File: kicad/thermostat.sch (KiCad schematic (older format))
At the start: 18 parts, among them J1 Display i2c, J2 Sensor i2c, J3 PoE Input, J4 PoE Output, J5 1827585-1

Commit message: Ready for checkout and routing
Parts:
- removed J5: 1827585-1, TE_1827585-1, symbol thermostat:1827585-1
- added J5: 0857891001, project_footprints:0857891001, symbol thermostat:0857891001
- J1: footprint Socket_Strips:Socket_Strip_Angled_1x04_Pitch2.54mm -> Pin_Headers:Pin_Header_Angled_1x04_Pitch2.54mm
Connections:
- net GND: now also J4.1 (Pin_1)
- net PWR_3.3V: no longer SW_DOWN1.2, SW_ENTER1.2, SW_MODE1.2, SW_UP1.2
- net PWR_5V: now also J4.2 (Pin_2), SW_DOWN1.2, SW_ENTER1.2, SW_MODE1.2, SW_UP1.2
- net at J3.1 (Pin_1): now also J5.17 (J11)
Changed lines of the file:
@@
 EESchema Schematic File Version 4
 LIBS:thermostat-cache
-EELAYER 30 0
+EELAYER 29 0
 EELAYER END
 $Descr A4 11693 8268
@@
 	2100 5650 2500 5650
 Text Label 2500 5650 0    50   ~ 0
-PWR_3.3V
+PWR_5V
 Text Label 2500 5200 0    50   ~ 0
-PWR_3.3V
+PWR_5V
 Text Label 2500 4750 0    50   ~ 0
-PWR_3.3V
+PWR_5V
 Text Label 2500 4300 0    50   ~ 0
-PWR_3.3V
+PWR_5V
 Wire Wire Line
 	1700 5650 850  5650
@@
 F 0 "J1" H 9580 3092 50  0000 L CNN
 F 1 "Display i2c" H 9580 3001 50  0000 L CNN
-F 2 "Socket_Strips:Socket_Strip_Angled_1x04_Pitch2.54mm" H 9500 3100 50  0001 C CNN
+F 2 "Pin_Headers:Pin_Header_Angled_1x04_Pitch2.54mm" H 9500 3100 50  0001 C CNN
 F 3 "~" H 9500 3100 50  0001 C CNN
 	1    9500 3100
@@
 F 3 "~" H 9500 3600 50  0001 C CNN
 	1    9500 3600
-	1    0    0    -1
-$EndComp
-$Comp
-L Connector_Generic:Conn_01x04 J3
-U 1 1 5D685426
-P 4850 5700
-F 0 "J3" H 4930 5692 50  0000 L CNN
-F 1 "PoE Input" H 4930 5601 50  0000 L CNN
-F 2 "Socket_Strips:Socket_Strip_Angled_1x04_Pitch2.54mm" H 4850 5700 50  0001 C CNN
-F 3 "~" H 4850 5700 50  0001 C CNN
-	1    4850 5700
-	-1   0    0    1
-$EndComp
-$Comp
-L Connector_Generic:Conn_01x04 J4
-U 1 1 5D687A2E
-P 4850 5100
-F 0 "J4" H 4930 5092 50  0000 L CNN
-F 1 "PoE Output" H 4930 5001 50  0000 L CNN
-F 2 "Socket_Strips:Socket_Strip_Angled_1x04_Pitch2.54mm" H 4850 5100 50  0001 C CNN
-F 3 "~" H 4850 5100 50  0001 C CNN
-	1    4850 5100
-	-1   0    0    1
-$EndComp
-$Comp
-L thermostat:1827585-1 J5
-U 1 1 5D644363
-P 5750 5350
-F 0 "J5" H 6029 5363 50  0000 L CNN
-F 1 "1827585-1" H 6029 5272 50  0000 L CNN
-F 2 "TE_1827585-1" H 5750 5350 50  0001 L BNN
-F 3 "Compliant" H 5750 5350 50  0001 L BNN
-F 4 "1827585-1" H 5750 5350 50  0001 L BNN "Field4"
-F 5 "https://www.te.com/usa-en/product-1827585-1.html?te_bu=Cor&te_type=disp&te_campaign=seda_glo_cor-seda-global-disp-prtnr-fy19-seda-model-bom-cta_sma-317_1&elqCampaignId=32493" H 5750 5350 50  0001 L BNN "Field5"
-F 6 "Conn RJ-45 F 8 POS 2.04mm Solder RA Thru-Hole 8 Terminal 1 Port Tray" H 5750 5350 50  0001 L BNN "Field6"
-F 7 "1827585-1" H 5750 5350 50  0001 L BNN "Field7"
-F 8 "Unavailable" H 5750 5350 50  0001 L BNN "Field8"
-F 9 "TE Connectivity" H 5750 5350 50  0001 L BNN "Field9"
-F 10 "None" H 5750 5350 50  0001 L BNN "Field10"
-F 11 "None" H 5750 5350 50  0001 L BNN "Field11"
-	1    5750 5350
 	1    0    0    -1
 $EndComp
@@
 Wire Wire Line
 	9300 3800 9100 3800
+$Comp
+L Connector_Generic:Conn_01x04 J4
+U 1 1 5D687A2E
+P 4850 5100
+F 0 "J4" H 4930 5092 50  0000 L CNN
+F 1 "PoE Output" H 4930 5001 50  0000 L CNN
+F 2 "Socket_Strips:Socket_Strip_Angled_1x04_Pitch2.54mm" H 4850 5100 50  0001 C CNN
+F 3 "~" H 4850 5100 50  0001 C CNN
+	1    4850 5100
+	-1   0    0    1
+$EndComp
+$Comp
+L Connector_Generic:Conn_01x04 J3
+U 1 1 5D685426
+P 4850 5700
+F 0 "J3" H 4930 5692 50  0000 L CNN
+F 1 "PoE Input" H 4930 5601 50  0000 L CNN
+F 2 "Socket_Strips:Socket_Strip_Angled_1x04_Pitch2.54mm" H 4850 5700 50  0001 C CNN
+F 3 "~" H 4850 5700 50  0001 C CNN
+	1    4850 5700
+	-1   0    0    1
+$EndComp
+$Comp
+L thermostat:0857891001 J5
+U 1 1 5D6600E3
+P 5950 5350
+F 0 "J5" H 5950 4635 50  0000 C CNN
+F 1 "0857891001" H 5950 4726 50  0000 C CNN
+F 2 "project_footprints:0857891001" H 5300 5100 50  0001 C CNN
+F 3 "" H 5300 5100 50  0001 C CNN
+	1    5950 5350
+	-1   0    0    1
+$EndComp
+Wire Wire Line
+	5550 5500 5300 5500
+Wire Wire Line
+	5300 5500 5300 5800
+Wire Wire Line
+	5300 5800 5050 5800
+Text Label 5200 5200 0    50   ~ 0
+GND
+Text Label 5200 5100 0    50   ~ 0
+PWR_5V
+Wire Wire Line
+	5050 5200 5200 5200
+Wire Wire Line
+	5050 5100 5200 5100
 $EndSCHEMATC

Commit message: Re-arrange board; still need measurements
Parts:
- J1: footprint Pin_Headers:Pin_Header_Angled_1x04_Pitch2.54mm -> Pin_Headers:Pin_Header_Straight_1x04_Pitch2.54mm
- J3, J4: footprint Socket_Strips:Socket_Strip_Angled_1x04_Pitch2.54mm -> Pin_Headers:Pin_Header_Straight_1x04_Pitch2.54mm
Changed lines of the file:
@@
 F 0 "J1" H 9580 3092 50  0000 L CNN
 F 1 "Display i2c" H 9580 3001 50  0000 L CNN
-F 2 "Pin_Headers:Pin_Header_Angled_1x04_Pitch2.54mm" H 9500 3100 50  0001 C CNN
+F 2 "Pin_Headers:Pin_Header_Straight_1x04_Pitch2.54mm" H 9500 3100 50  0001 C CNN
 F 3 "~" H 9500 3100 50  0001 C CNN
 	1    9500 3100
@@
 F 0 "J4" H 4930 5092 50  0000 L CNN
 F 1 "PoE Output" H 4930 5001 50  0000 L CNN
-F 2 "Socket_Strips:Socket_Strip_Angled_1x04_Pitch2.54mm" H 4850 5100 50  0001 C CNN
+F 2 "Pin_Headers:Pin_Header_Straight_1x04_Pitch2.54mm" H 4850 5100 50  0001 C CNN
 F 3 "~" H 4850 5100 50  0001 C CNN
 	1    4850 5100
@@
 F 0 "J3" H 4930 5692 50  0000 L CNN
 F 1 "PoE Input" H 4930 5601 50  0000 L CNN
-F 2 "Socket_Strips:Socket_Strip_Angled_1x04_Pitch2.54mm" H 4850 5700 50  0001 C CNN
+F 2 "Pin_Headers:Pin_Header_Straight_1x04_Pitch2.54mm" H 4850 5700 50  0001 C CNN
 F 3 "~" H 4850 5700 50  0001 C CNN
 	1    4850 5700

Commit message: more updates, backstop before 24v conversation
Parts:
- J3, J4: footprint Pin_Headers:Pin_Header_Straight_1x04_Pitch2.54mm -> project_footprints:M20-7910542R; symbol Connector_Generic:Conn_01x04 -> Connector_Generic:Conn_01x05
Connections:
- net GND: now also J4.2 (Pin_2); no longer J4.1 (Pin_1)
- net PWR_5V: now also J4.3 (Pin_3); no longer J4.2 (Pin_2)
- net at J5.17 (J11): now also J3.2 (Pin_2); no longer J3.1 (Pin_1)
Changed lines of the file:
@@
 	9300 3800 9100 3800
 $Comp
-L Connector_Generic:Conn_01x04 J4
+L Connector_Generic:Conn_01x05 J4
 U 1 1 5D687A2E
 P 4850 5100
 F 0 "J4" H 4930 5092 50  0000 L CNN
 F 1 "PoE Output" H 4930 5001 50  0000 L CNN
-F 2 "Pin_Headers:Pin_Header_Straight_1x04_Pitch2.54mm" H 4850 5100 50  0001 C CNN
+F 2 "project_footprints:M20-7910542R" H 4850 5100 50  0001 C CNN
 F 3 "~" H 4850 5100 50  0001 C CNN
 	1    4850 5100
@@
 $EndComp
 $Comp
-L Connector_Generic:Conn_01x04 J3
+L Connector_Generic:Conn_01x05 J3
 U 1 1 5D685426
 P 4850 5700
 F 0 "J3" H 4930 5692 50  0000 L CNN
 F 1 "PoE Input" H 4930 5601 50  0000 L CNN
-F 2 "Pin_Headers:Pin_Header_Straight_1x04_Pitch2.54mm" H 4850 5700 50  0001 C CNN
+F 2 "project_footprints:M20-7910542R" H 4850 5700 50  0001 C CNN
 F 3 "~" H 4850 5700 50  0001 C CNN
 	1    4850 5700

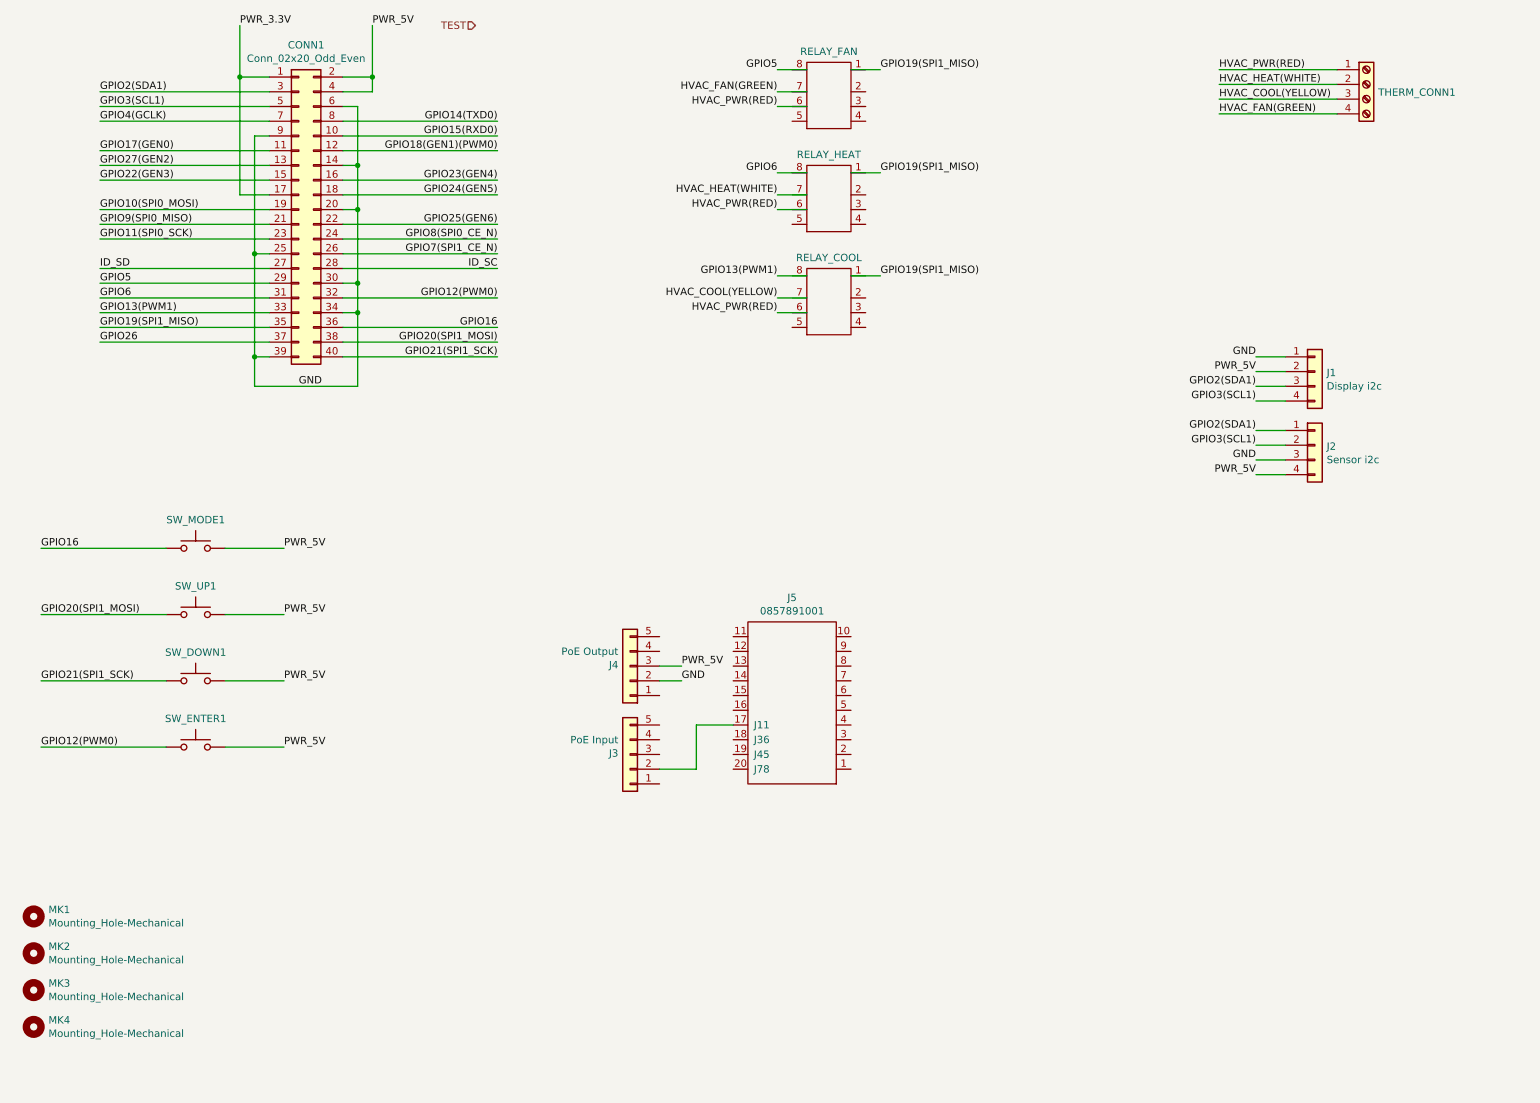
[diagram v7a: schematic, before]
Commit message: migrate to 24v conversion
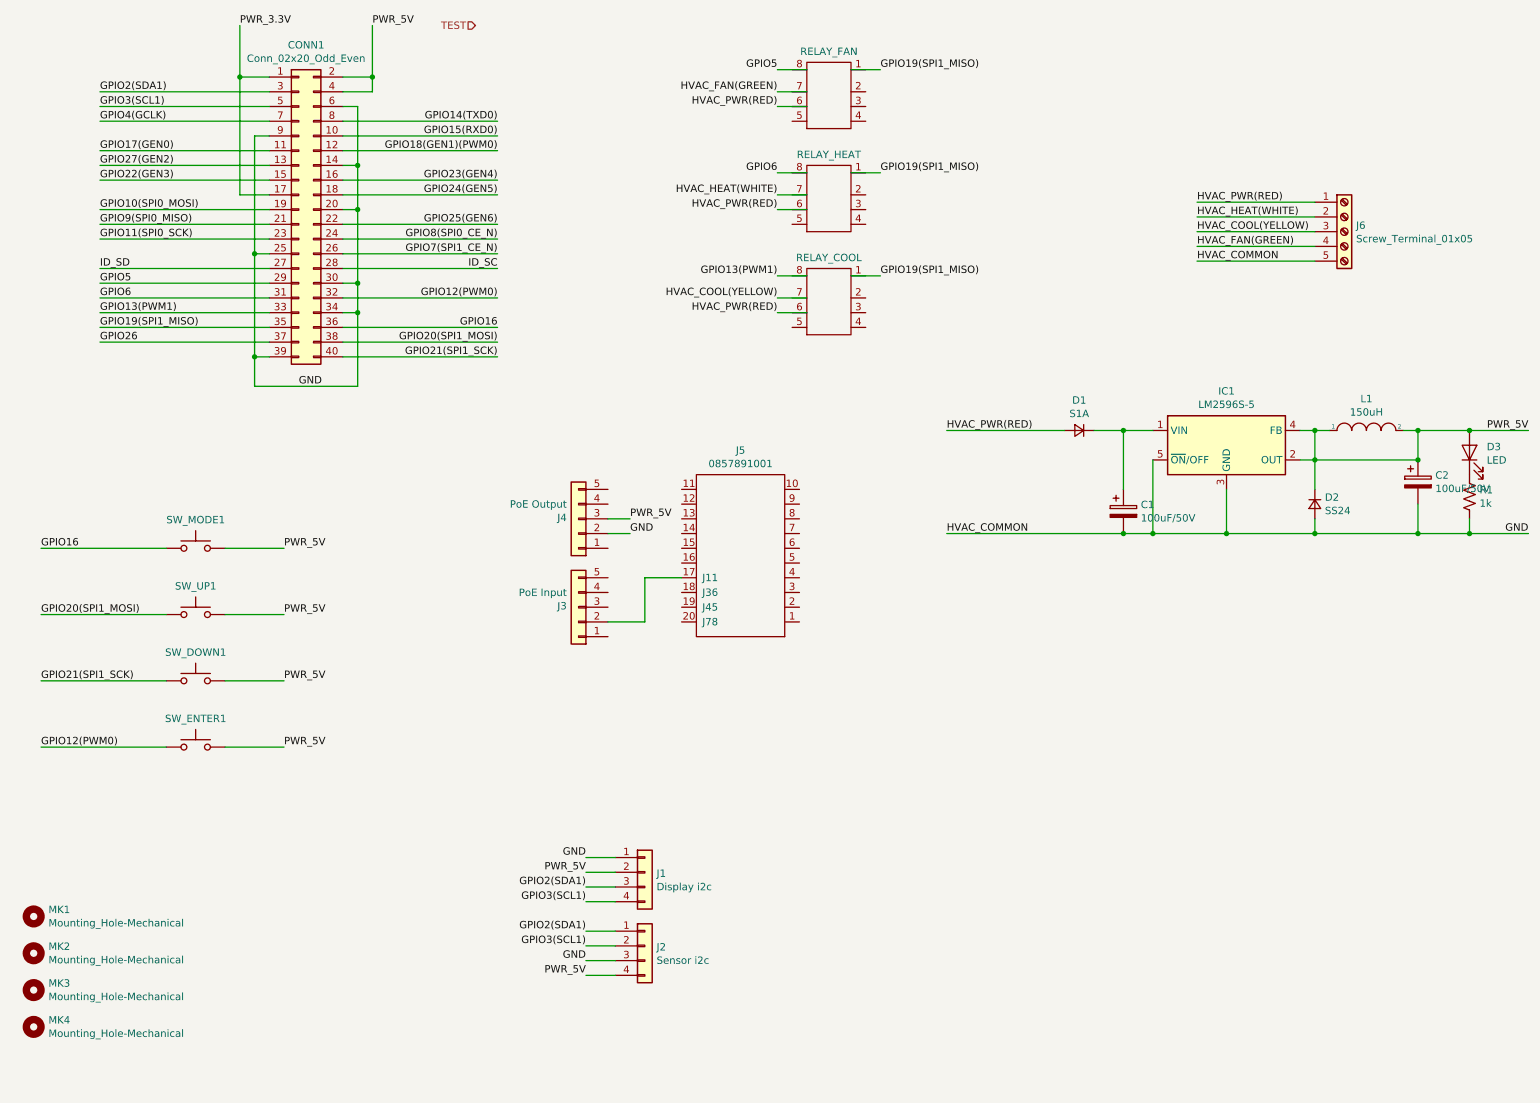
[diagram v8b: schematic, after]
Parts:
- removed THERM_CONN1: THERM_CONN, TerminalBlocks_Phoenix:TerminalBlock_Phoenix_MPT-2.54mm_4pol, symbol Connector:Screw_Terminal_01x04
- added C1, C2: 100uF/50V, Capacitors_SMD:CP_Elec_8x10, symbol Device:CP
- added D1: S1A, Diodes_SMD:D_SOD-123F, symbol Device:D_Small
- added D2: SS24, Diodes_SMD:D_SMB, symbol Device:D_Small
- added D3: LED, LEDs:LED_0805, symbol Device:LED
- added IC1: LM2596S-5, Package_TO_SOT_SMD:TO-263-5_TabPin3, symbol Regulator_Switching:LM2596S-5
- added J6: Screw_Terminal_01x05, symbol Connector:Screw_Terminal_01x05
- added L1: 150uH, Inductors_SMD:L_Neosid_Ms95a, symbol pspice:INDUCTOR
- added R1: 1k, Resistors_SMD:R_0805, symbol Device:R_US
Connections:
- net GND: now also C1.2, C2.2, D2.2 (A), IC1.3 (GND), IC1.5 (~ON~/OFF), J6.5 (Pin_5), R1.2
- net HVAC_COOL(YELLOW): now also J6.3 (Pin_3)
- net HVAC_FAN(GREEN): now also J6.4 (Pin_4)
- net HVAC_HEAT(WHITE): now also J6.2 (Pin_2)
- net HVAC_PWR(RED): now also D1.2 (A), J6.1 (Pin_1)
- net PWR_5V: now also C2.1, D2.1 (K), D3.2 (A), IC1.2 (OUT), IC1.4 (FB), L1.1, L1.2
- new net: C1.1, D1.1 (K), IC1.1 (VIN)
- new net: D3.1 (K), R1.1
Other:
- moved on the sheet: J1, J2, J3, J4, J5
